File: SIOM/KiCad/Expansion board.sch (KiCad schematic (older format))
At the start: 33 parts, among them Q801 BSS138, Q802 BSS138, U801 LM7332, U802 MAX3226, U803 SC16IS740, U804 MAX13432EESD, Y801 7.3728MHz

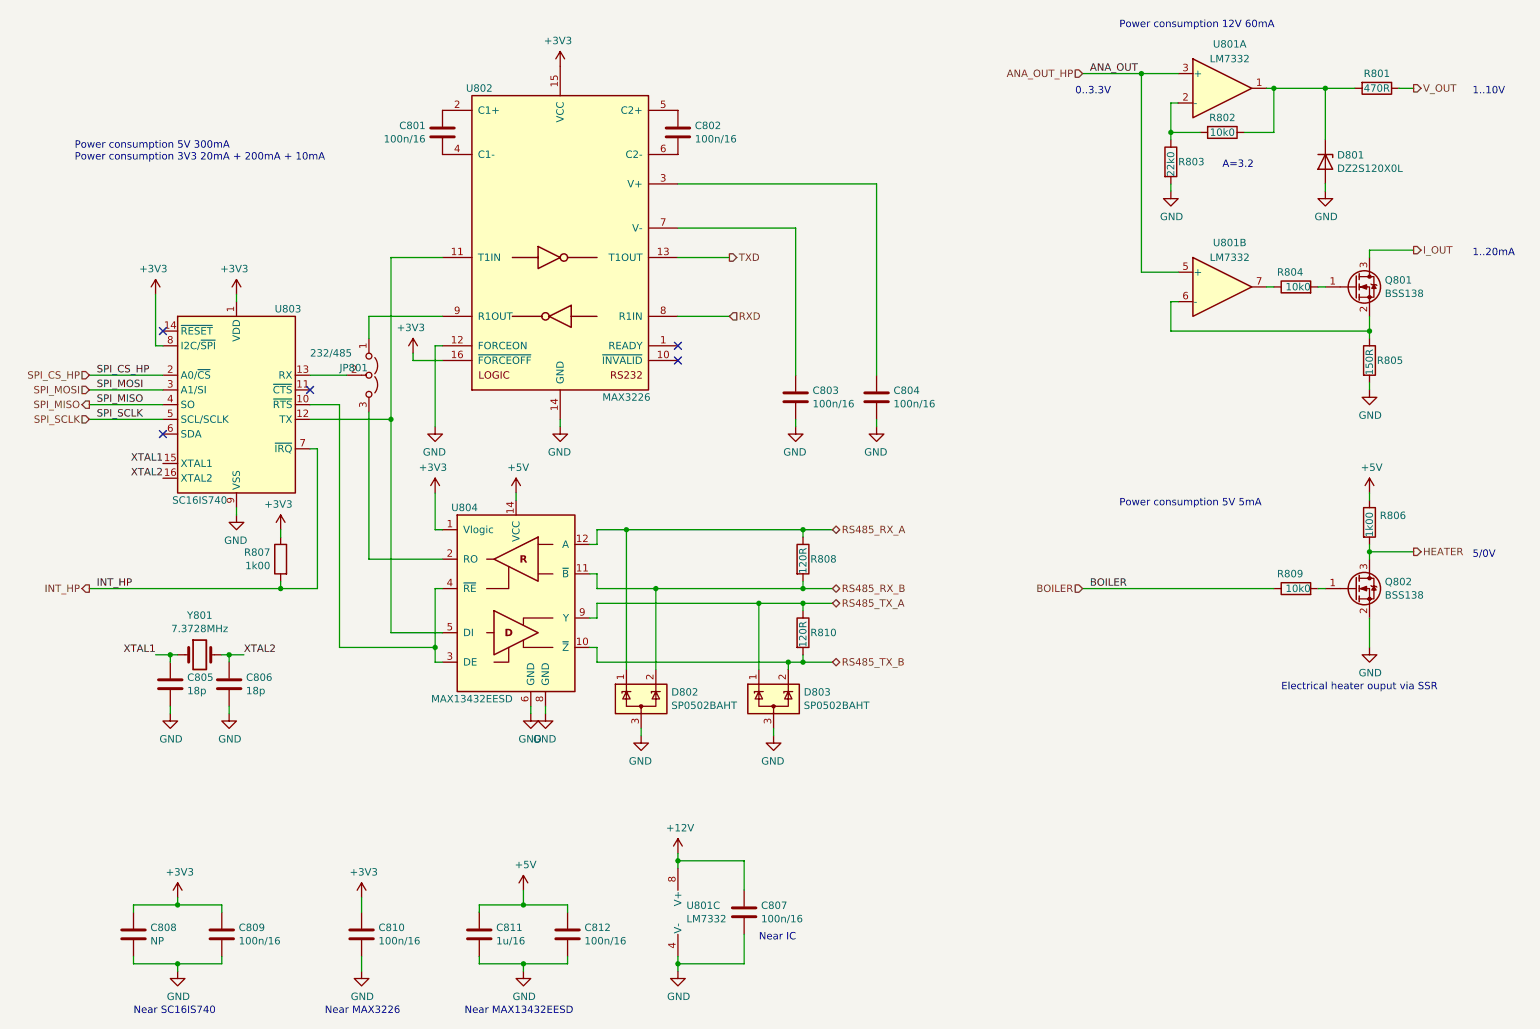
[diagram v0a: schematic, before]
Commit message: KiCad files SIOM_def
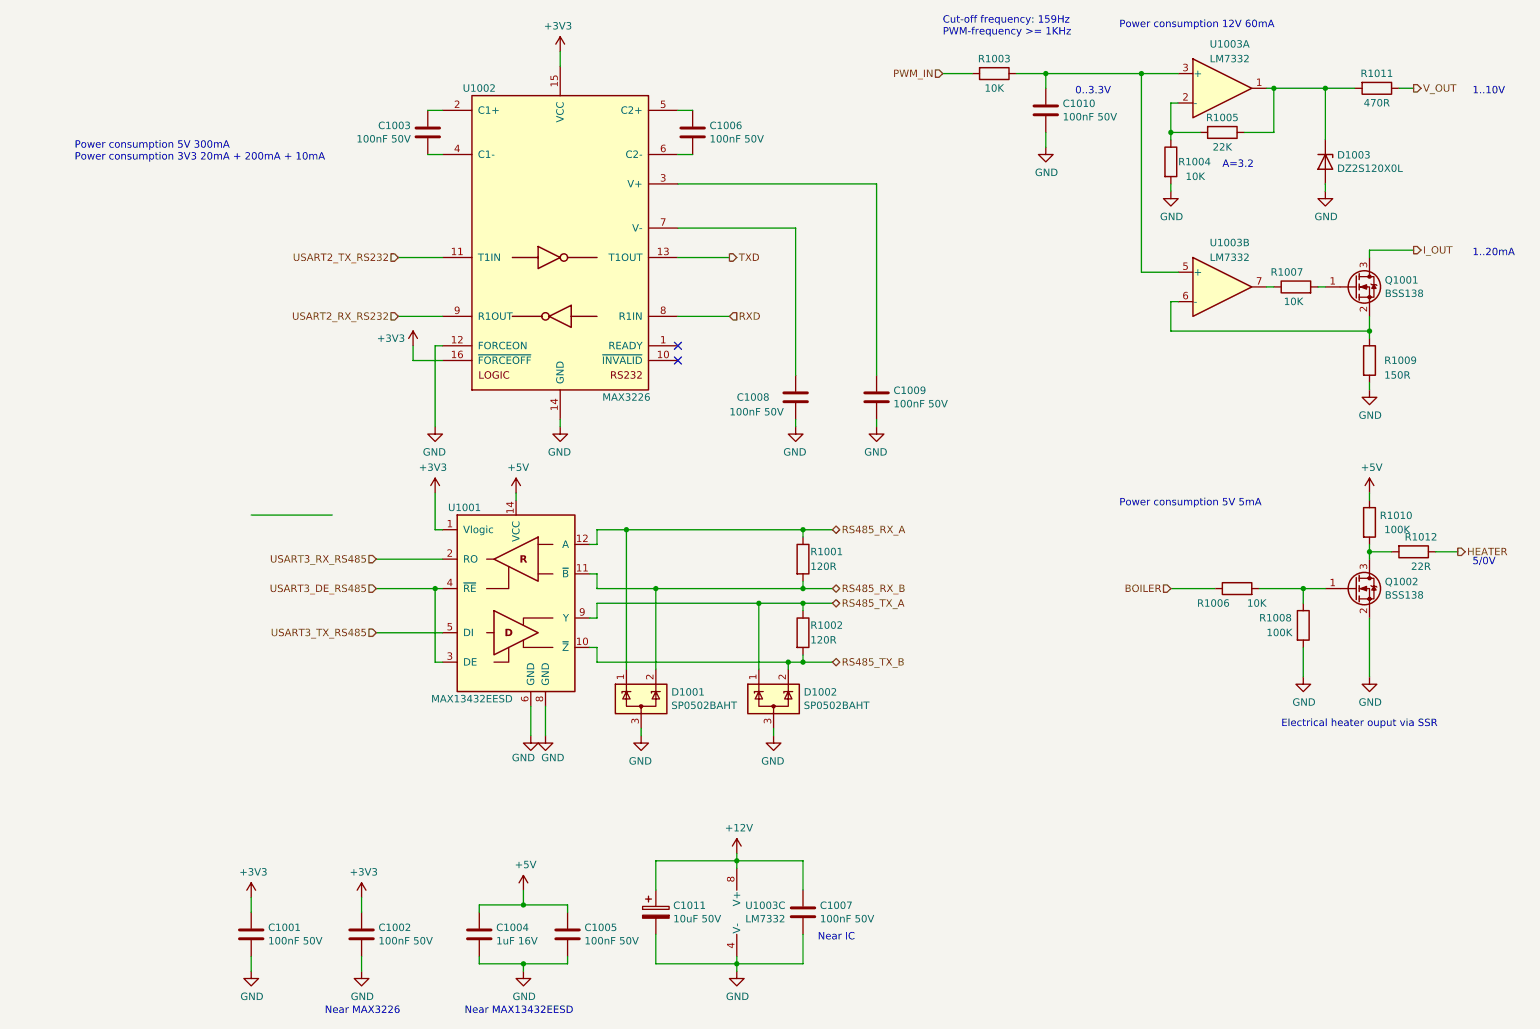
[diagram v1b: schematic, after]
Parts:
- removed C805, C806: 18p, Capacitor_SMD:C_0603_1608Metric, symbol SIOMv01-rescue:C-Device
- removed C808: NP, Capacitor_SMD:C_0805_2012Metric, symbol SIOMv01-rescue:C-Device
- removed C809: 100n/16, Capacitor_SMD:C_0603_1608Metric, symbol SIOMv01-rescue:C-Device
- removed JP801: 232/485, Connector_PinHeader_2.54mm:PinHeader_1x03_P2.54mm_Vertical, symbol Jumper:Jumper_3_Open
- removed R807: 1k00, Resistor_SMD:R_0603_1608Metric, symbol SIOMv01-rescue:R-Device
- removed U803: SC16IS740, Package_SO:TSSOP-16_4.4x5mm_P0.65mm, symbol SIOMv01-rescue:SC16IS740-Interface_UART
- removed Y801: 7.3728MHz, Crystal:Crystal_SMD_3225-4Pin_3.2x2.5mm, symbol SIOMv01-rescue:Crystal-Device
- added C1001, C1010: 100nF 50V, Capacitor_SMD:C_0603_1608Metric, symbol SIOMv01-rescue:C-Device
- added C1011: 10uF 50V, Capacitor_SMD:CP_Elec_5x5.3, symbol Device:CP
- added R1003: 10K, Resistor_SMD:R_0603_1608Metric, symbol SIOMv01-rescue:R-Device
- added R1008: 100K, Resistor_SMD:R_0603_1608Metric, symbol SIOMv01-rescue:R-Device
- added R1012: 22R, Resistor_SMD:R_2512_6332Metric_Pad1.40x3.35mm_HandSolder, symbol Device:R
- C1002: renamed from C810; value 100n/16 -> 100nF 50V
- C1003: renamed from C801; value 100n/16 -> 100nF 50V
- C1004: renamed from C811; value 1u/16 -> 1uF 16V
- C1005: renamed from C812; value 100n/16 -> 100nF 50V
- C1006: renamed from C802; value 100n/16 -> 100nF 50V
- C1007: renamed from C807; value 100n/16 -> 100nF 50V
- C1008: renamed from C803; value 100n/16 -> 100nF 50V
- C1009: renamed from C804; value 100n/16 -> 100nF 50V
- R1004: renamed from R803; value 22k0 -> 10K
- R1005: renamed from R802; value 10k0 -> 22K
- R1006: renamed from R809; value 10k0 -> 10K
- R1007: renamed from R804; value 10k0 -> 10K
- R1010: renamed from R806; value 1k00 -> 100K
- renumbered D802 to D1001, D803 to D1002, D801 to D1003, Q801 to Q1001, Q802 to Q1002, R808 to R1001, R810 to R1002, R805 to R1009, R801 to R1011, U804 to U1001, U802 to U1002, U801 to U1003
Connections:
- net +12V: now also C1011.1
- net +3V3: now also C1001.1
- net GND: now also C1001.2, C1010.2, C1011.2, R1008.2
- net HEATER: now also R1012.1; no longer Q1002.3 (D), R1010.2
- net USART3_DE_RS485: now reaches U1001.3 (DE), U1001.4 (~RE)
- net USART2_TX_RS232: now reaches U1002.11 (T1IN)
- net USART2_TX_RS232: no longer U1001.5 (DI)
- net USART2_RX_RS232: now reaches U1002.9 (R1OUT)
- net USART3_RX_RS485: now reaches U1001.2 (RO)
- net at Q1002.1 (G), R1006.2: now also R1008.1
- net ANA_OUT_HP: no longer names the net of U1003.3 (+), U1003.5 (+)
- net ANA_OUT_HP: now also C1010.1, R1003.1
- new net: Q1002.3 (D), R1010.2, R1012.2
- new net PWM_IN: R1003.2
- new net USART3_TX_RS485: U1001.5 (DI)
- no-connect marks 5 -> 2
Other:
- note added: "Cut-off frequency: 159Hz\nPWM-frequency >= 1KHz"
- note removed: "Near SC16IS740"
- moved on the sheet: C1003, C1006, C1007, R1006, U1003C
